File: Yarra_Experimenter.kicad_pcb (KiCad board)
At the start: 2 copper layers, 70 x 35 mm, 148 parts

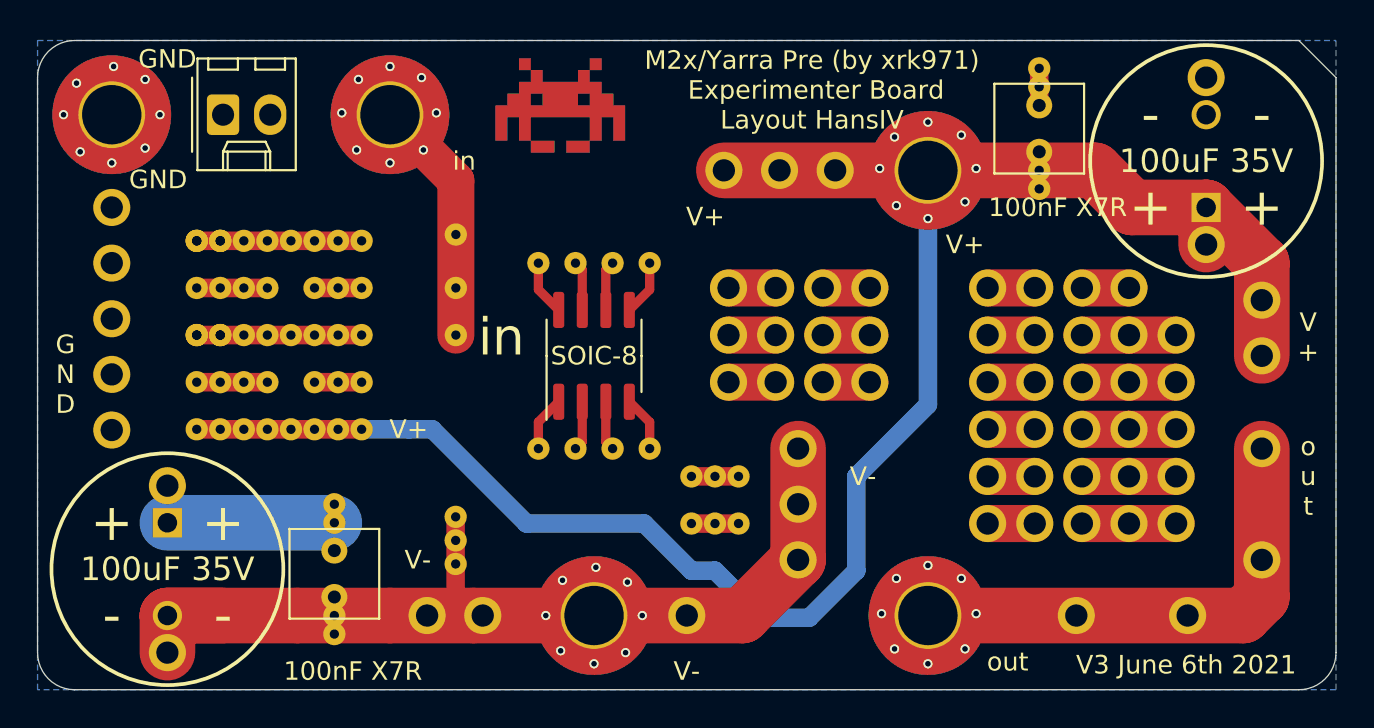
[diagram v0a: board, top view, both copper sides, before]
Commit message: Moved mounting /signal holes location to correct position
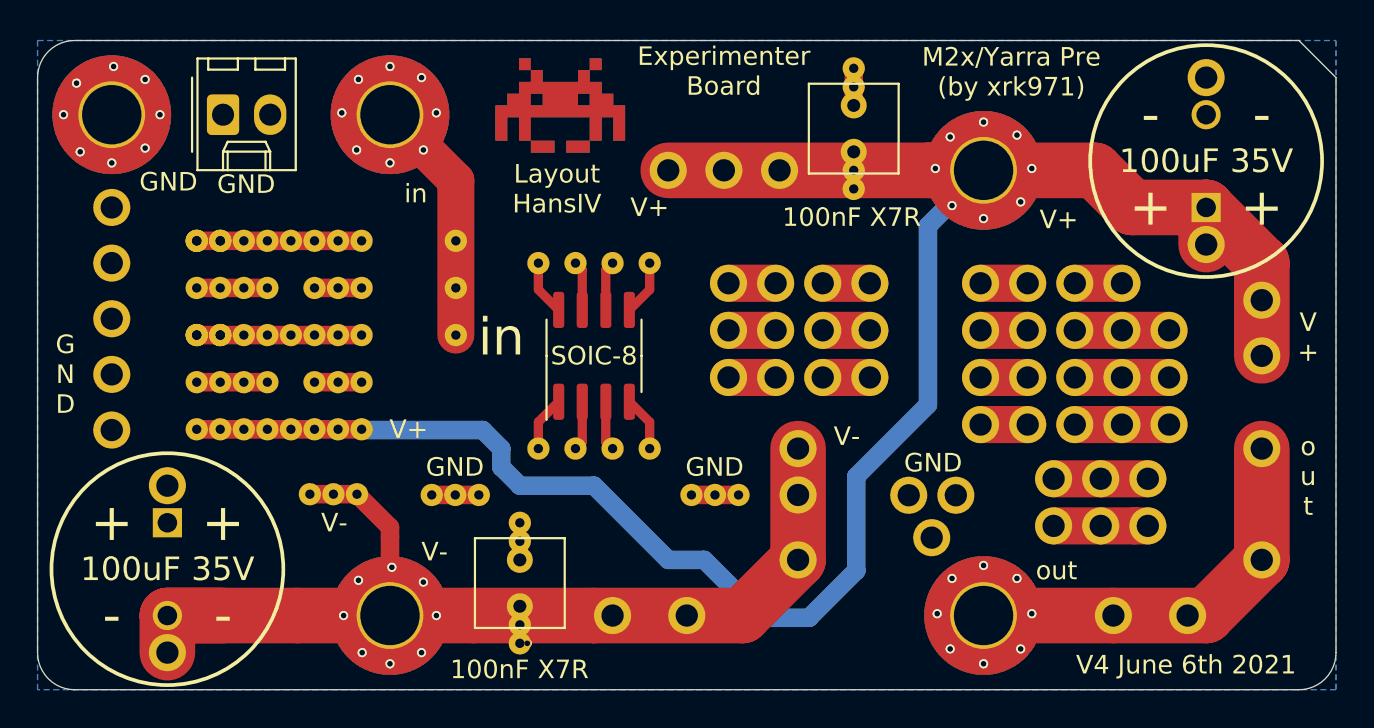
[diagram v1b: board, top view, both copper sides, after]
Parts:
- removed the REF** at (84.0, 71.0)
- removed the REF** at (95.2, 66.0)
- removed the REF** at (96.5, 66.0)
- removed the REF** at (97.8, 66.0)
- removed the REF** at (111.2, 66.0)
- added REF**: VIA_1mm, SamacSys_Parts:VIA_1mm, F.Cu at (83.8, 64.5)
- added REF**: VIA_1mm, SamacSys_Parts:VIA_1mm, F.Cu at (82.5, 64.5)
- added REF**: VIA_1mm, SamacSys_Parts:VIA_1mm, F.Cu at (81.2, 64.5)
- moved H2 11.0 mm to (79.0, 71.0)
- moved REF** 10.1 mm to (86.0, 72.5)
- moved REF** 10.0 mm to (86.0, 66.0)
- moved REF** 10.0 mm to (86.0, 67.0)
- moved C3 10.0 mm to (86.0, 70.5)
- moved REF** 10.0 mm to (86.0, 71.5)
- moved C4 10.0 mm to (104.0, 46.0)
- moved REF** 10.0 mm to (104.0, 48.0)
- moved REF** 10.0 mm to (104.0, 47.0)
- moved REF** 10.0 mm to (104.0, 41.5)
- moved REF** 10.0 mm to (104.0, 42.5)
- moved REF** 10.0 mm to (91.0, 71.0)
- moved REF** 7.95 mm to (74.7, 64.5), turned to 180 degrees
- moved REF** 7.04 mm to (76.0, 64.5), turned to 180 degrees
- moved REF** 6.51 mm to (77.2, 64.5), turned to 180 degrees
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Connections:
- REF** pad 1: (no net) -> Net-(C1-Pad2) (x4)
- REF** pad 1: (no net) -> GNDREF (x6)
- REF** pad 1: (no net) -> Net-(H4-Pad1) (x4)
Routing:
- net (no net): track 116.6 -> 106.4 mm
- net Net-(C2-Pad1): track 102.1 -> 108.9 mm
- net Net-(H4-Pad1): track 26.4 -> 22.0 mm
- net Net-(C1-Pad2): track 52.0 -> 56.1 mm, vias 8 -> 9
- net GNDREF: track 11.0 -> 7.08 mm
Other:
- board text added: "Experimenter Board"
- board text added: "GND"
- board text added: "Layout HansIV"
- board text added: "M2x/Yarra Pre (by xrk971)"
- board text added: "V4 June 6th 2021"
- board text removed: "M2x/Yarra Pre (by xrk971) Experimenter Board Layout HansIV"
- board text removed: "V3 June 6th 2021"
